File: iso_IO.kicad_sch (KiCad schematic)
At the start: 32 parts, among them J9 AVR-ISP-6, Q7 Q_NMOS_GDS, U10 AM26LV32xD, U11 ADuM120N1, U12 ADuM120N1, U13 PC355, U9 ATtiny13A-SU

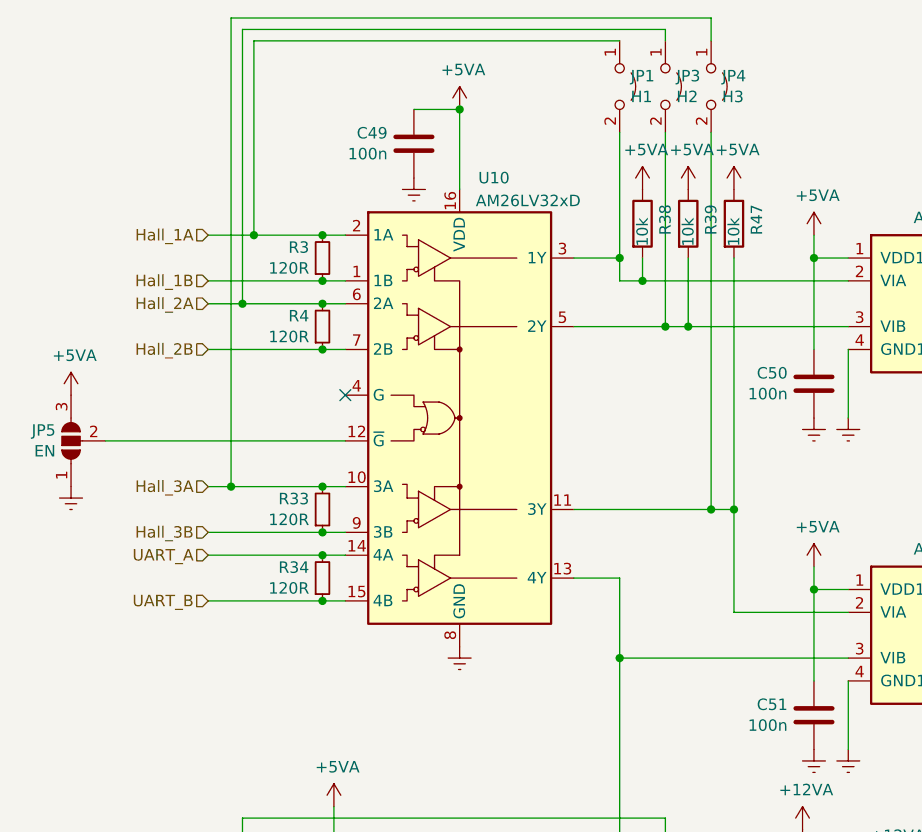
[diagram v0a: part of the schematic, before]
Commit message: - peeled back the filler planes around HV logic - improved insulation on HV logic
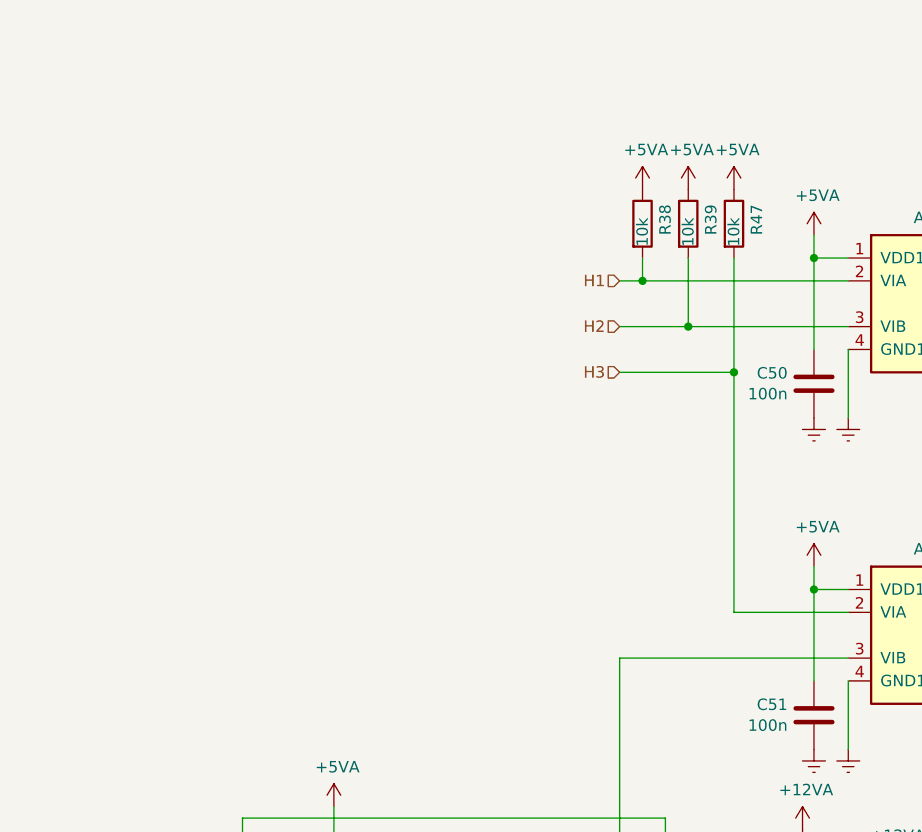
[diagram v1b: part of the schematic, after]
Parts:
- removed C49: 100n, Capacitor_SMD:C_0805_2012Metric, symbol Device:C
- removed JP1: H1, Jumper:SolderJumper-2_P1.3mm_Open_TrianglePad1.0x1.5mm, symbol Jumper:Jumper_2_Open
- removed JP3: H2, Jumper:SolderJumper-2_P1.3mm_Open_TrianglePad1.0x1.5mm, symbol Jumper:Jumper_2_Open
- removed JP4: H3, Jumper:SolderJumper-2_P1.3mm_Open_TrianglePad1.0x1.5mm, symbol Jumper:Jumper_2_Open
- removed JP5: EN, Jumper:SolderJumper-3_P2.0mm_Open_TrianglePad1.0x1.5mm, symbol HSWR-rescue:SolderJumper_3_Open-Jumper
- removed R3, R33, R34, R4: 120R, Resistor_SMD:R_0805_2012Metric, symbol Device:R_Small
- removed U10: AM26LV32xD, Package_SO:SOIC-16_3.9x9.9mm_P1.27mm, symbol Interface:AM26LV32xD
- U9: footprint Package_SO:SOIJ-8_5.3x5.3mm_P1.27mm -> Package_SO:SOIC-8W_5.3x5.3mm_P1.27mm
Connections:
- net H1: now reaches R38.2, U11.2 (VIA)
- net H2: now reaches R39.2, U11.3 (VIB)
- net H3: now reaches R47.2, U12.2 (VIA)
- no-connect marks 1 -> 0
